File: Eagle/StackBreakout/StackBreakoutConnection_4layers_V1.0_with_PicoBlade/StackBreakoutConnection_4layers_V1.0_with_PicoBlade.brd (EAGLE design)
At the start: 96 x 89.9 mm, 13 parts, among them J1 SSQ-126-23-G-D, J2 SSQ-126-23-G-D

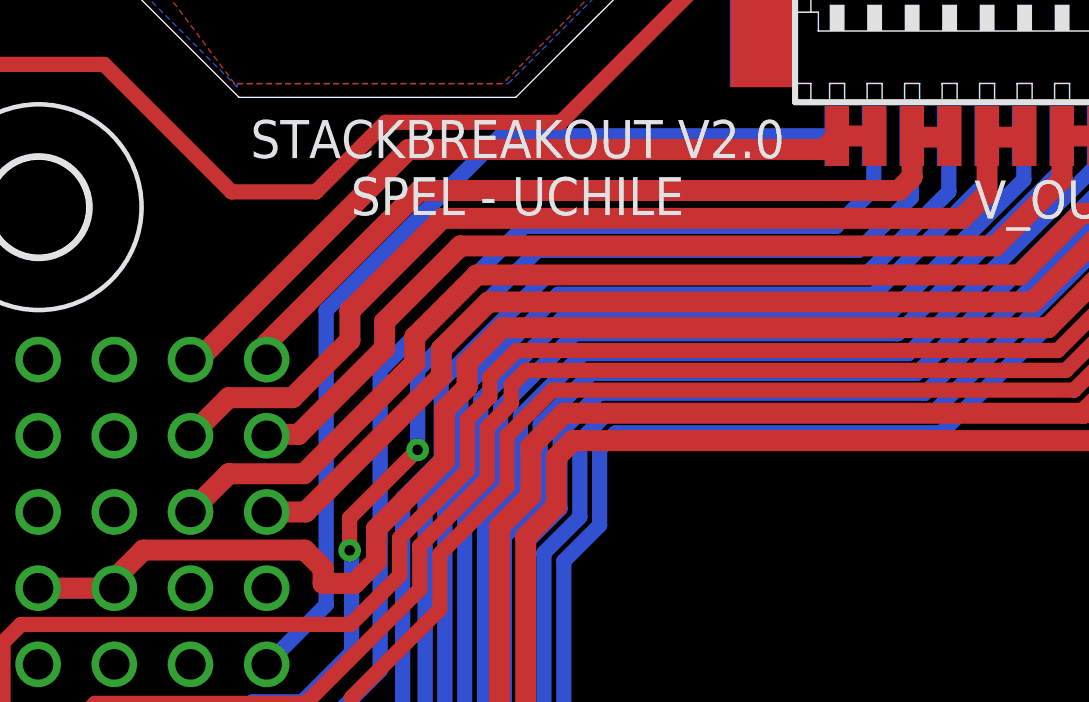
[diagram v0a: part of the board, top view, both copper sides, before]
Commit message: Output voltage pin update
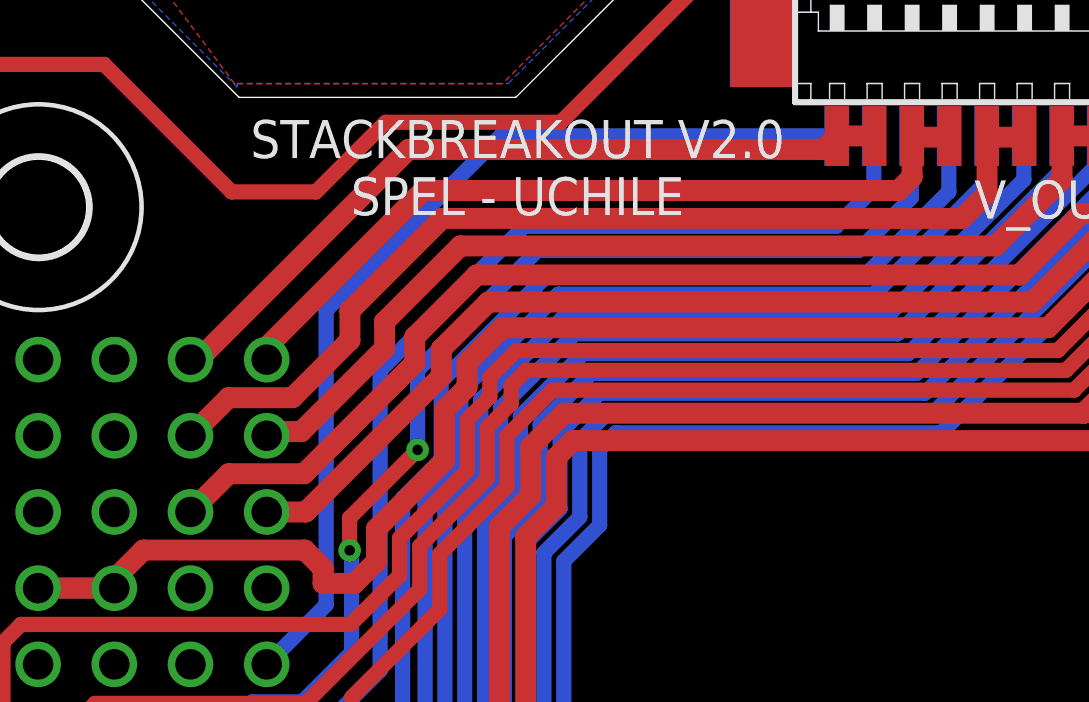
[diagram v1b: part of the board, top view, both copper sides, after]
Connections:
- net OUT1_3V3 renamed OUT-0
- net OUT2_3V3 renamed OUT-1
- net OUT3_3V3 renamed OUT-2
- net OUT4_5V0 renamed OUT-3
- net OUT5_5V0 renamed OUT-4
- net OUT6_5V0 renamed OUT-5

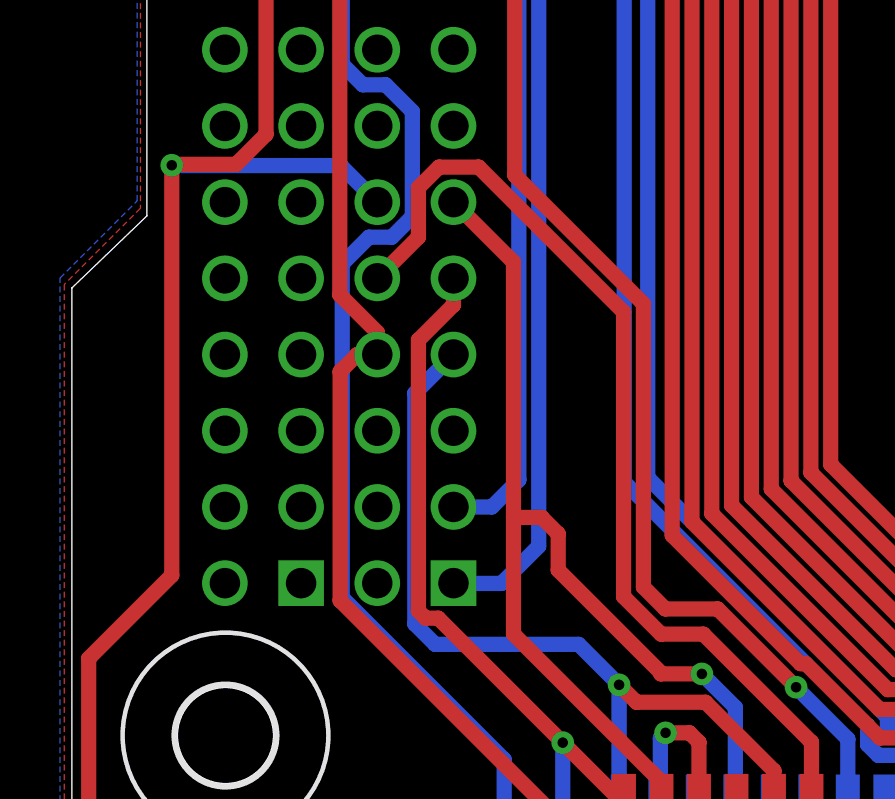
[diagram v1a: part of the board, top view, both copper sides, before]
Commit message: update i2c pinout
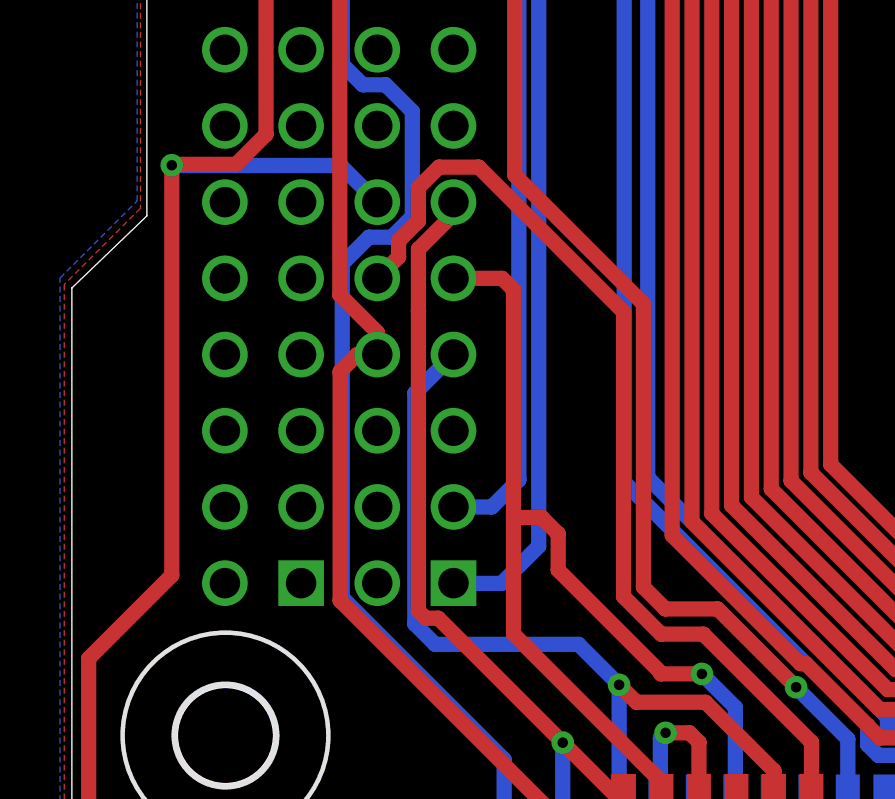
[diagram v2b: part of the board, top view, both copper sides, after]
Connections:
- net I2C2_SCL2: now also J1.9; no longer J1.11
- net I2C2_SDA2: now also J1.11; no longer J1.9
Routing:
- net I2C2_SDA2: track 30.9 -> 33.4 mm
- net I2C2_SCL2: track 36.9 -> 35.3 mm
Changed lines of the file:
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@@
 <wire x1="11.5516" y1="26.34396875" x2="12.23603125" y2="27.0284" width="0.508" layer="1"/>
 <wire x1="12.23603125" y1="27.0284" x2="13.5616" y2="27.0284" width="0.508" layer="1"/>
-<wire x1="10.18" y1="23.32" x2="11.5516" y2="24.6916" width="0.508" layer="1"/>
-<wire x1="11.5516" y1="24.6916" x2="11.5516" y2="26.34396875" width="0.508" layer="1"/>
 <wire x1="18.39" y1="22.2" x2="18.39" y2="12.71" width="0.508" layer="1"/>
 <wire x1="18.39" y1="12.71" x2="19.64" y2="11.46" width="0.508" layer="1"/>
@@
 <wire x1="24.653" y1="3.893" x2="24.653" y2="5.802" width="0.508" layer="1"/>
 <wire x1="24.15" y1="3.39" x2="24.653" y2="3.893" width="0.508" layer="1"/>
+<wire x1="10.18" y1="23.32" x2="10.8912" y2="24.0312" width="0.508" layer="1"/>
+<wire x1="10.8912" y1="24.0312" x2="10.8912" y2="24.56515" width="0.508" layer="1"/>
+<wire x1="10.8912" y1="24.56515" x2="11.5516" y2="25.22555" width="0.508" layer="1"/>
+<wire x1="11.5516" y1="25.22555" x2="11.5516" y2="26.34396875" width="0.508" layer="1"/>
 </signal>
 <signal name="GSSB_VCC2">
@@
 <signal name="I2C2_SCL2">
 <contactref element="GSSB_I2C_IN" pad="2"/>
-<contactref element="J1" pad="11"/>
 <contactref element="SPI-GSSB" pad="9"/>
 <wire x1="19.653" y1="5.802" x2="19.6594" y2="5.8084" width="0.508" layer="1"/>
 <wire x1="19.6594" y1="6.5203375" x2="19.6594" y2="5.8084" width="0.508" layer="1"/>
 <wire x1="19.6594" y1="6.5203375" x2="14.72" y2="11.4597375" width="0.508" layer="1"/>
-<wire x1="14.72" y1="23.86" x2="12.72" y2="25.86" width="0.508" layer="1"/>
 <wire x1="14.72" y1="11.4597375" x2="14.72" y2="15.35" width="0.508" layer="1"/>
-<wire x1="14.72" y1="15.35" x2="14.72" y2="23.86" width="0.508" layer="1"/>
+<wire x1="14.72" y1="15.35" x2="14.72" y2="22.94" width="0.508" layer="1"/>
 <wire x1="22.115" y1="5.782" x2="22.115" y2="9.0196" width="0.508" layer="16"/>
 <wire x1="22.115" y1="9.0196" x2="21" y2="10.1346" width="0.508" layer="16"/>
@@
 <wire x1="16.2104" y1="14.80355" x2="15.66395" y2="15.35" width="0.508" layer="1"/>
 <wire x1="15.66395" y1="15.35" x2="14.72" y2="15.35" width="0.508" layer="1"/>
+<contactref element="J1" pad="9"/>
+<wire x1="14.72" y1="22.94" x2="14.34" y2="23.32" width="0.508" layer="1"/>
+<wire x1="14.34" y1="23.32" x2="12.72" y2="23.32" width="0.508" layer="1"/>
 </signal>
 <signal name="I2C2_SDA2">
 <contactref element="GSSB_I2C_IN" pad="1"/>
-<contactref element="J1" pad="9"/>
 <contactref element="SPI-GSSB" pad="10"/>
 <wire x1="11.7896625" y1="11.9916" x2="11.5516" y2="12.2296625" width="0.508" layer="1"/>
 <wire x1="12.2134" y1="11.9916" x2="11.7896625" y2="11.9916" width="0.508" layer="1"/>
-<wire x1="12.72" y1="22.43236875" x2="12.72" y2="23.32" width="0.508" layer="1"/>
 <wire x1="18.403" y1="5.802" x2="16.3625" y2="7.8425" width="0.508" layer="1"/>
 <wire x1="16.3625" y1="7.8425" x2="12.2134" y2="11.9916" width="0.508" layer="1"/>
-<wire x1="11.5516" y1="21.26396875" x2="12.72" y2="22.43236875" width="0.508" layer="1"/>
-<wire x1="11.5516" y1="12.2296625" x2="11.5516" y2="21.26396875" width="0.508" layer="1"/>
+<wire x1="11.5516" y1="22.22396875" x2="11.56" y2="22.23236875" width="0.508" layer="1"/>
+<wire x1="11.5516" y1="12.2296625" x2="11.5516" y2="22.22396875" width="0.508" layer="1"/>
 <wire x1="20.865" y1="5.782" x2="20.865" y2="4.105" width="0.508" layer="16"/>
 <wire x1="20.865" y1="4.105" x2="20.03" y2="3.27" width="0.508" layer="16"/>
@@
 <via x="16.3625" y="7.8425" extent="1-16" drill="0.35"/>
 <wire x1="18.62" y1="3.27" x2="16.3625" y2="5.5275" width="0.508" layer="16"/>
+<contactref element="J1" pad="11"/>
+<wire x1="11.5516" y1="22.22396875" x2="11.5516" y2="24.2916" width="0.508" layer="1"/>
+<wire x1="12.72" y1="25.46" x2="12.72" y2="25.86" width="0.508" layer="1"/>
+<wire x1="11.5516" y1="24.2916" x2="12.72" y2="25.46" width="0.508" layer="1"/>
 </signal>
 <signal name="SPI0_CS1">
